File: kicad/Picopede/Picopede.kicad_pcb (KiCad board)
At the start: 2 copper layers, 20.3 x 90 mm, 4 parts

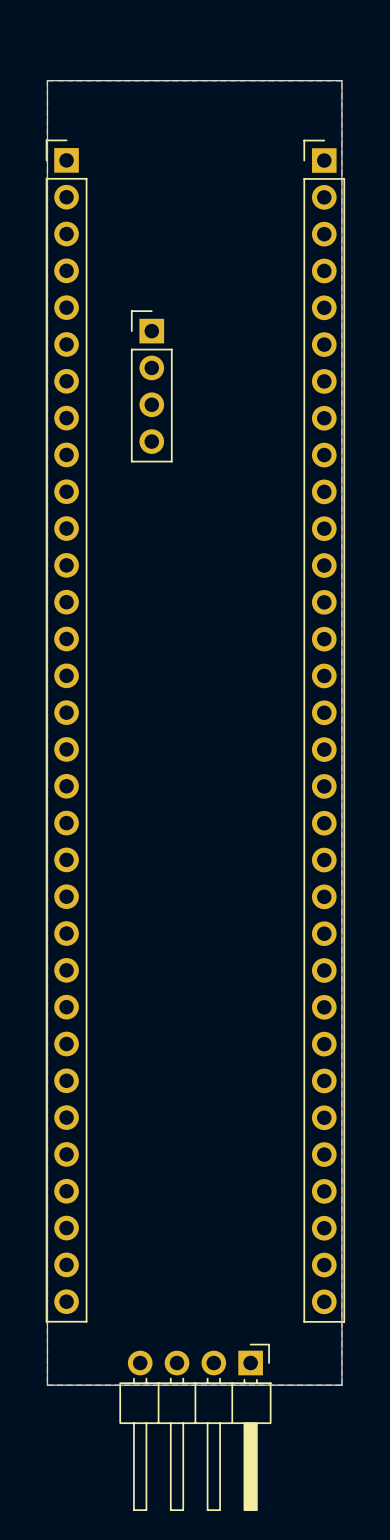
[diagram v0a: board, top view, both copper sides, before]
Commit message: cleaned up schematic
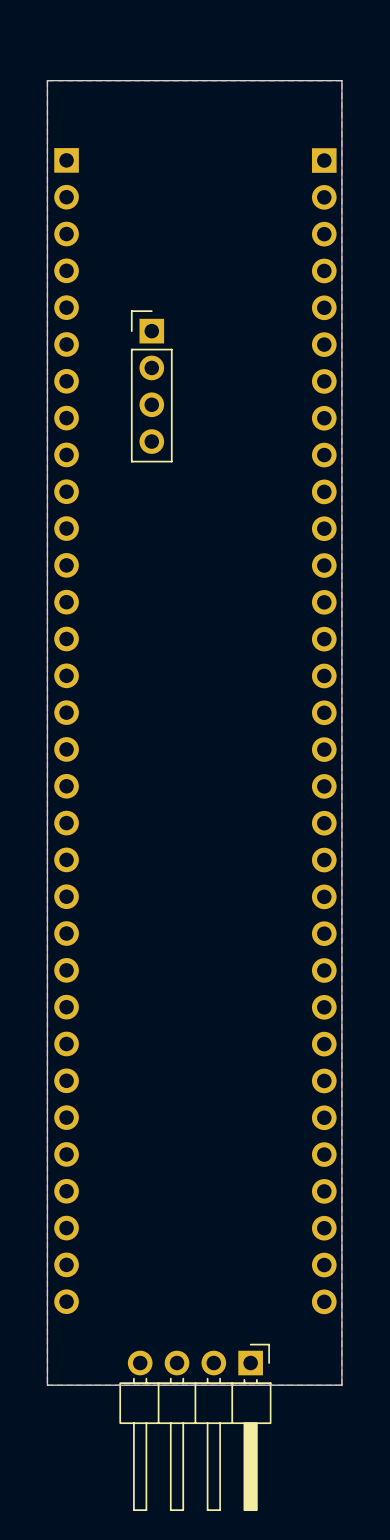
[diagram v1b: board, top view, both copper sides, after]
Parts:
- REF** (x2): moved to B.Cu
- turned REF** to 180 degrees (x2)

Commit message: mount holes added
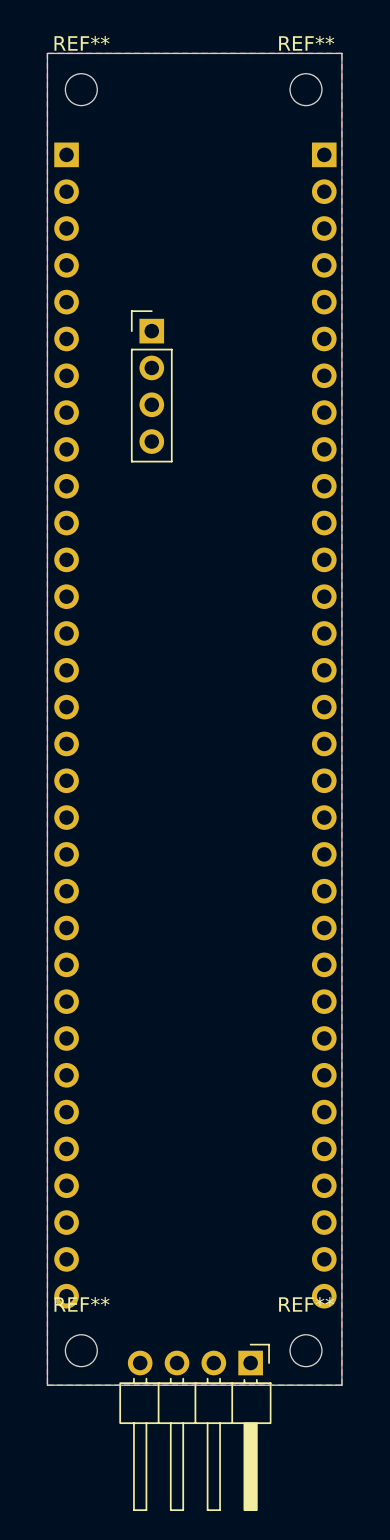
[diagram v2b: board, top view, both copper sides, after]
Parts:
- added REF**: MountingHole_2.2mm_M2, MountingHole:MountingHole_2.2mm_M2, F.Cu at (155.5, 135.5)
- added REF**: MountingHole_2.2mm_M2, MountingHole:MountingHole_2.2mm_M2, F.Cu at (140.0, 135.5)
- added REF**: MountingHole_2.2mm_M2, MountingHole:MountingHole_2.2mm_M2, F.Cu at (155.5, 48.5)
- added REF**: MountingHole_2.2mm_M2, MountingHole:MountingHole_2.2mm_M2, F.Cu at (140.0, 48.5)
- moved REF** 0.39 mm to (156.8, 53.0)
- moved REF** 0.38 mm to (139.0, 53.0)
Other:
- board size 20.3 x 90 mm -> 20.3 x 91.9 mm

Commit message: header foodprints
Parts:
- removed the REF** at (156.8, 53.0)
- removed the REF** at (139.0, 53.0)
- added REF**: PinHeader_1x32_P2.54mm_Vertical, Connector_PinHeader_2.54mm:PinHeader_1x32_P2.54mm_Vertical, B.Cu at (138.9, 52.8)
- added REF**: PinHeader_1x32_P2.54mm_Vertical, Connector_PinHeader_2.54mm:PinHeader_1x32_P2.54mm_Vertical, B.Cu at (156.7, 52.8)
- moved REF** 4.20 mm to (144.8, 61.0)
- moved REF** 1.00 mm to (155.5, 134.5)
- moved REF** 1.00 mm to (140.1, 134.5)
- moved REF** 0.85 mm to (151.7, 135.5)
- moved REF** 0.20 mm to (155.7, 48.5)
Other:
- board size 20.3 x 91.9 mm -> 20.3 x 91 mm
